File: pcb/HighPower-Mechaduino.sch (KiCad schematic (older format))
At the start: 31 parts, among them J1 SUPPLY, J2 STEPPER, P1 SWD, Q1 SSM3J328R, Q2 BSS138, SW1 SW_PUSH, U1 AS5047D, U2 AP2112K-3.3TRG1, U3 AT24CS64-SSHM

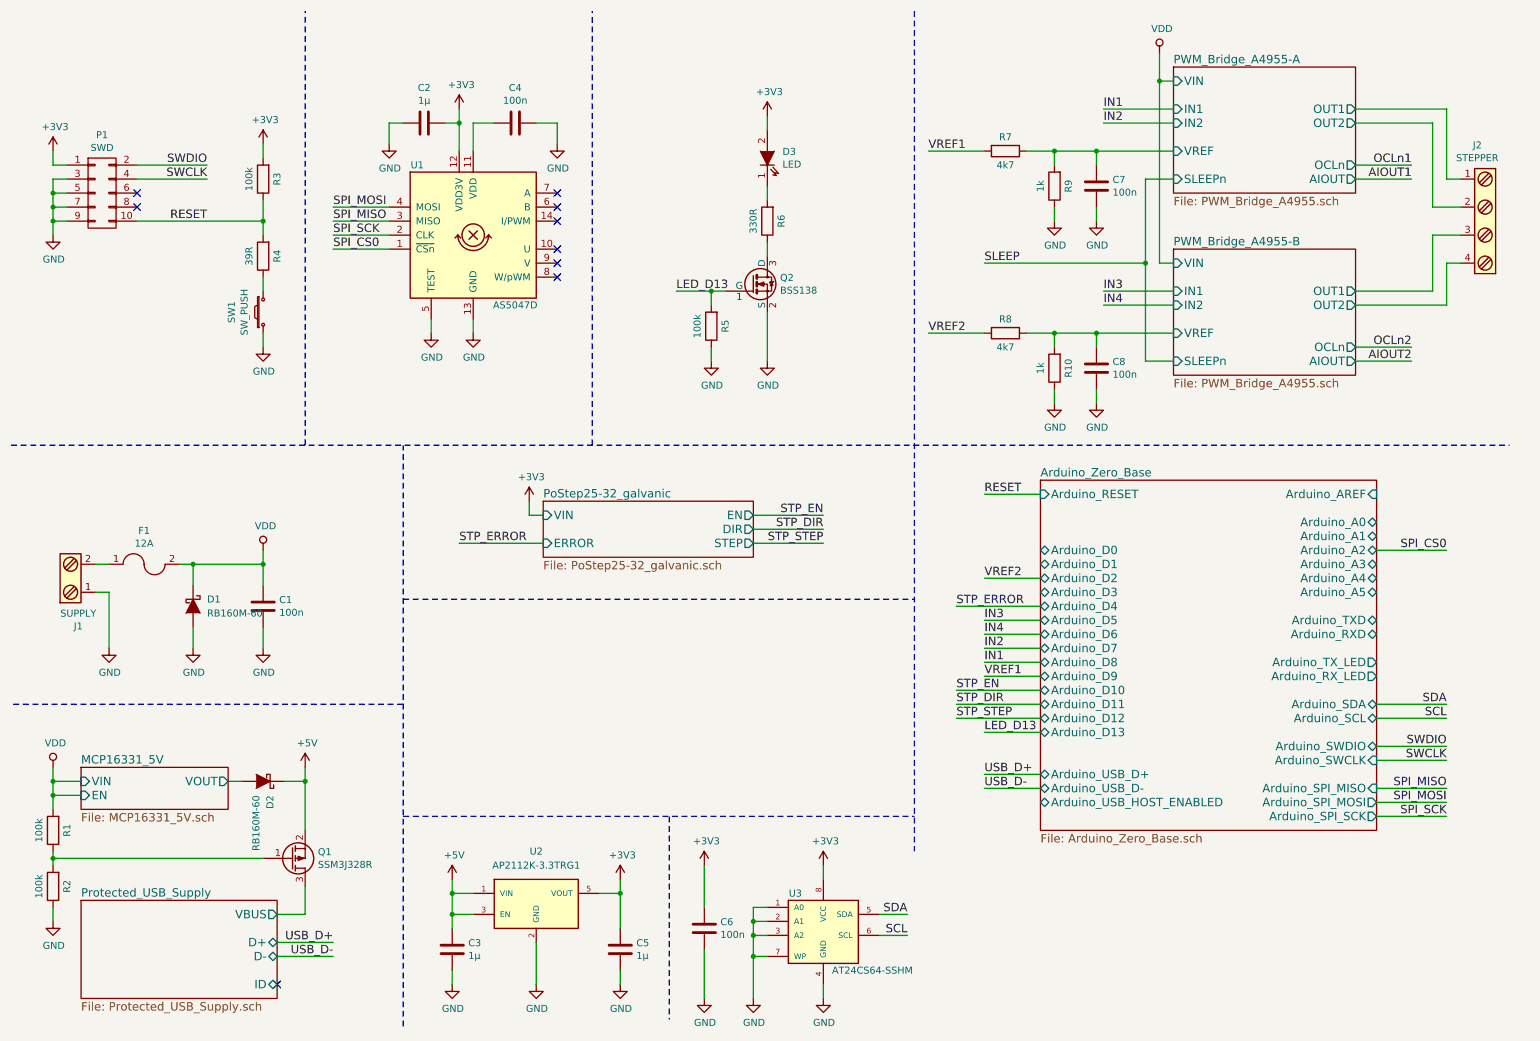
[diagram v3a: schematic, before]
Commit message: Improve pcb routing, add testpoints and etc. The design improves a lot. Still lots to do, but most important design parts should now be drafted almost complete.
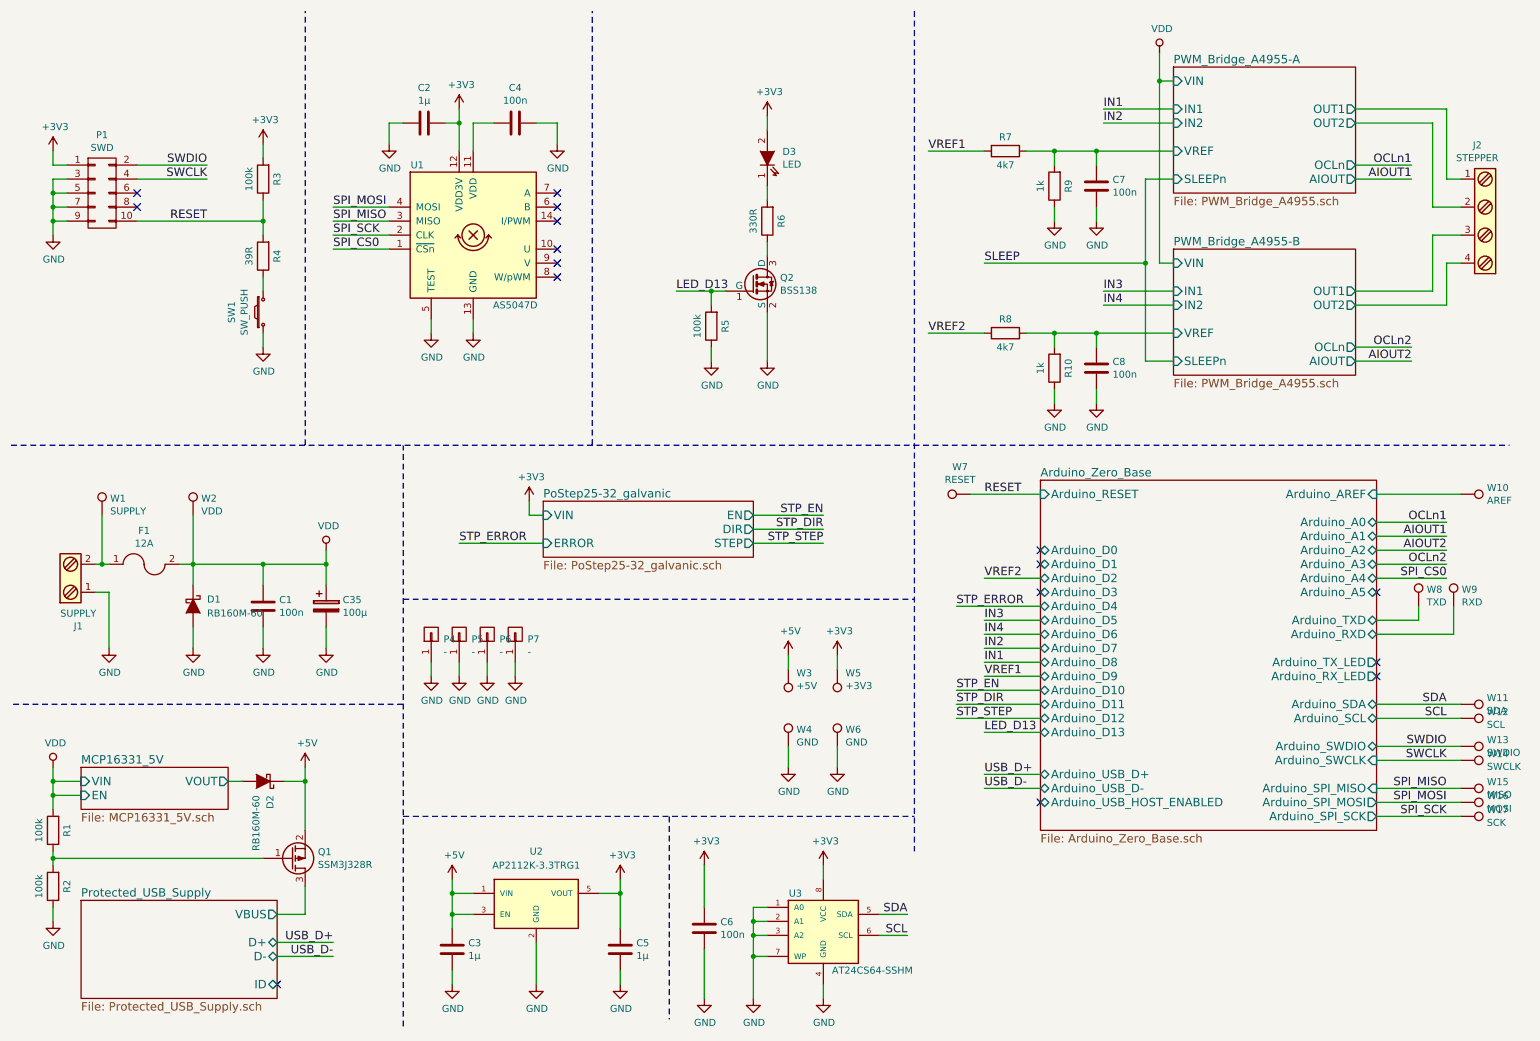
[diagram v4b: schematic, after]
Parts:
- added C35: 100µ, Capacitors_SMD:c_elec_10x10, symbol CP
- added P4, P5, P6, P7: -, Mounting_Holes:MountingHole_4.3mm_M4_Pad_Via, symbol CONN_01X01
- added W1: SUPPLY, Measurement_Points:Measurement_Point_Round-SMD-Pad_Small, symbol TEST_1P
- added W10: AREF, Measurement_Points:Measurement_Point_Round-SMD-Pad_Small, symbol TEST_1P
- added W11: SDA, Measurement_Points:Measurement_Point_Round-SMD-Pad_Small, symbol TEST_1P
- added W12: SCL, Measurement_Points:Measurement_Point_Round-SMD-Pad_Small, symbol TEST_1P
- added W13: SWDIO, Measurement_Points:Measurement_Point_Round-SMD-Pad_Small, symbol TEST_1P
- added W14: SWCLK, Measurement_Points:Measurement_Point_Round-SMD-Pad_Small, symbol TEST_1P
- added W15: MISO, Measurement_Points:Measurement_Point_Round-SMD-Pad_Small, symbol TEST_1P
- added W16: MOSI, Measurement_Points:Measurement_Point_Round-SMD-Pad_Small, symbol TEST_1P
- added W17: SCK, Measurement_Points:Measurement_Point_Round-SMD-Pad_Small, symbol TEST_1P
- added W2: VDD, Measurement_Points:Measurement_Point_Round-SMD-Pad_Small, symbol TEST_1P
- added W3: +5V, Measurement_Points:Measurement_Point_Round-SMD-Pad_Small, symbol TEST_1P
- added W4, W6: GND, Measurement_Points:Measurement_Point_Round-SMD-Pad_Small, symbol TEST_1P
- added W5: +3V3, Measurement_Points:Measurement_Point_Round-SMD-Pad_Small, symbol TEST_1P
- added W7: RESET, Measurement_Points:Measurement_Point_Round-SMD-Pad_Small, symbol TEST_1P
- added W8: TXD, Measurement_Points:Measurement_Point_Round-SMD-Pad_Small, symbol TEST_1P
- added W9: RXD, Measurement_Points:Measurement_Point_Round-SMD-Pad_Small, symbol TEST_1P
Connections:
- net +3V3: now also W5.1
- net +5V: now also W3.1
- net Arduino_Zero_Base/Arduino_AREF: now also W10.1
- net Arduino_Zero_Base/Arduino_RXD: now also W9.1
- net Arduino_Zero_Base/Arduino_TXD: now also W8.1
- net GND: now also C35.2, P4.1 (P1), P5.1 (P1), P6.1 (P1), P7.1 (P1), W4.1, W6.1
- net RESET: now also W7.1
- net SCL: now also W12.1
- net SDA: now also W11.1
- net SPI_MISO: now also W15.1
- net SPI_MOSI: now also W16.1
- net SPI_SCK: now also W17.1
- net SWCLK: now also W14.1
- net SWDIO: now also W13.1
- net VDD: now also C35.1, W2.1
- net at F1.1, J1.2: now also W1.1
- no-connect marks 9 -> 16

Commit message: Improve pcb
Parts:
- F1: footprint Fuse_Holders_and_Fuses:Fuseholder5x20_horiz_open_inline_Type-I -> Fuse_Holders_and_Fuses_local:Fuse_0679H
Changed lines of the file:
@@
 F 0 "F1" H 1450 4690 50  0000 C CNN
 F 1 "12A" H 1450 4599 50  0000 C CNN
-F 2 "Fuse_Holders_and_Fuses:Fuseholder5x20_horiz_open_inline_Type-I" H 1450 4450 50  0001 C CNN
+F 2 "Fuse_Holders_and_Fuses_local:Fuse_0679H" H 1450 4450 50  0001 C CNN
 F 3 "" H 1450 4450 50  0000 C CNN
 	1    1450 4450

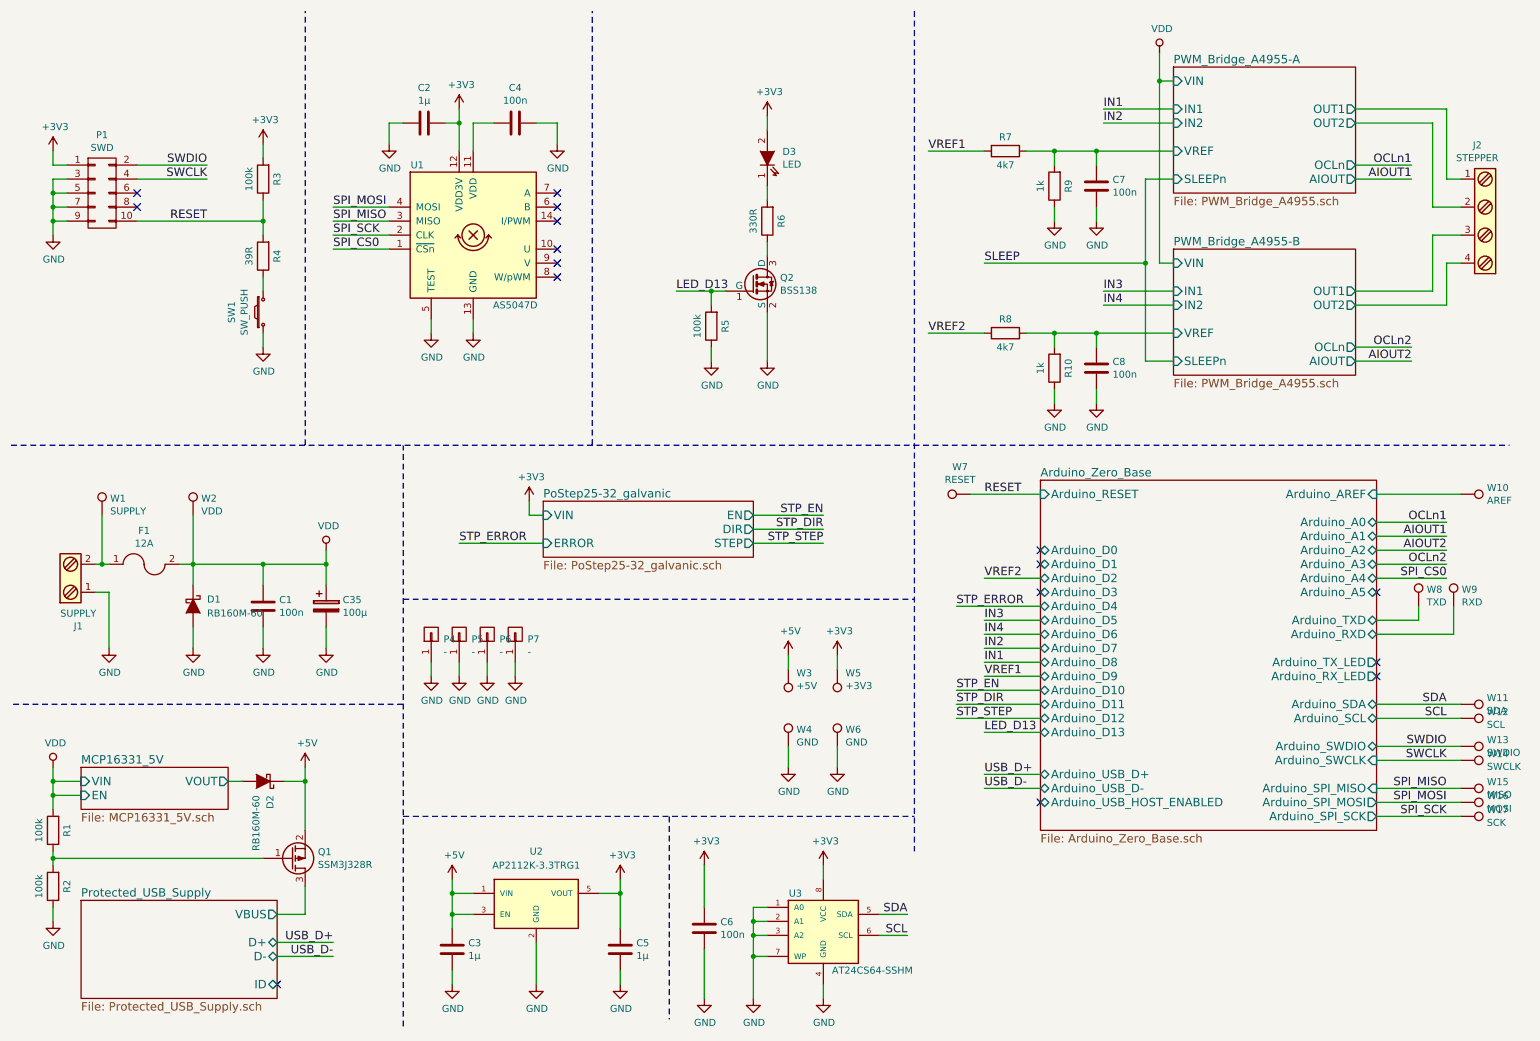
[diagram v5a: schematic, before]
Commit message: Improve board routing, add some dukos
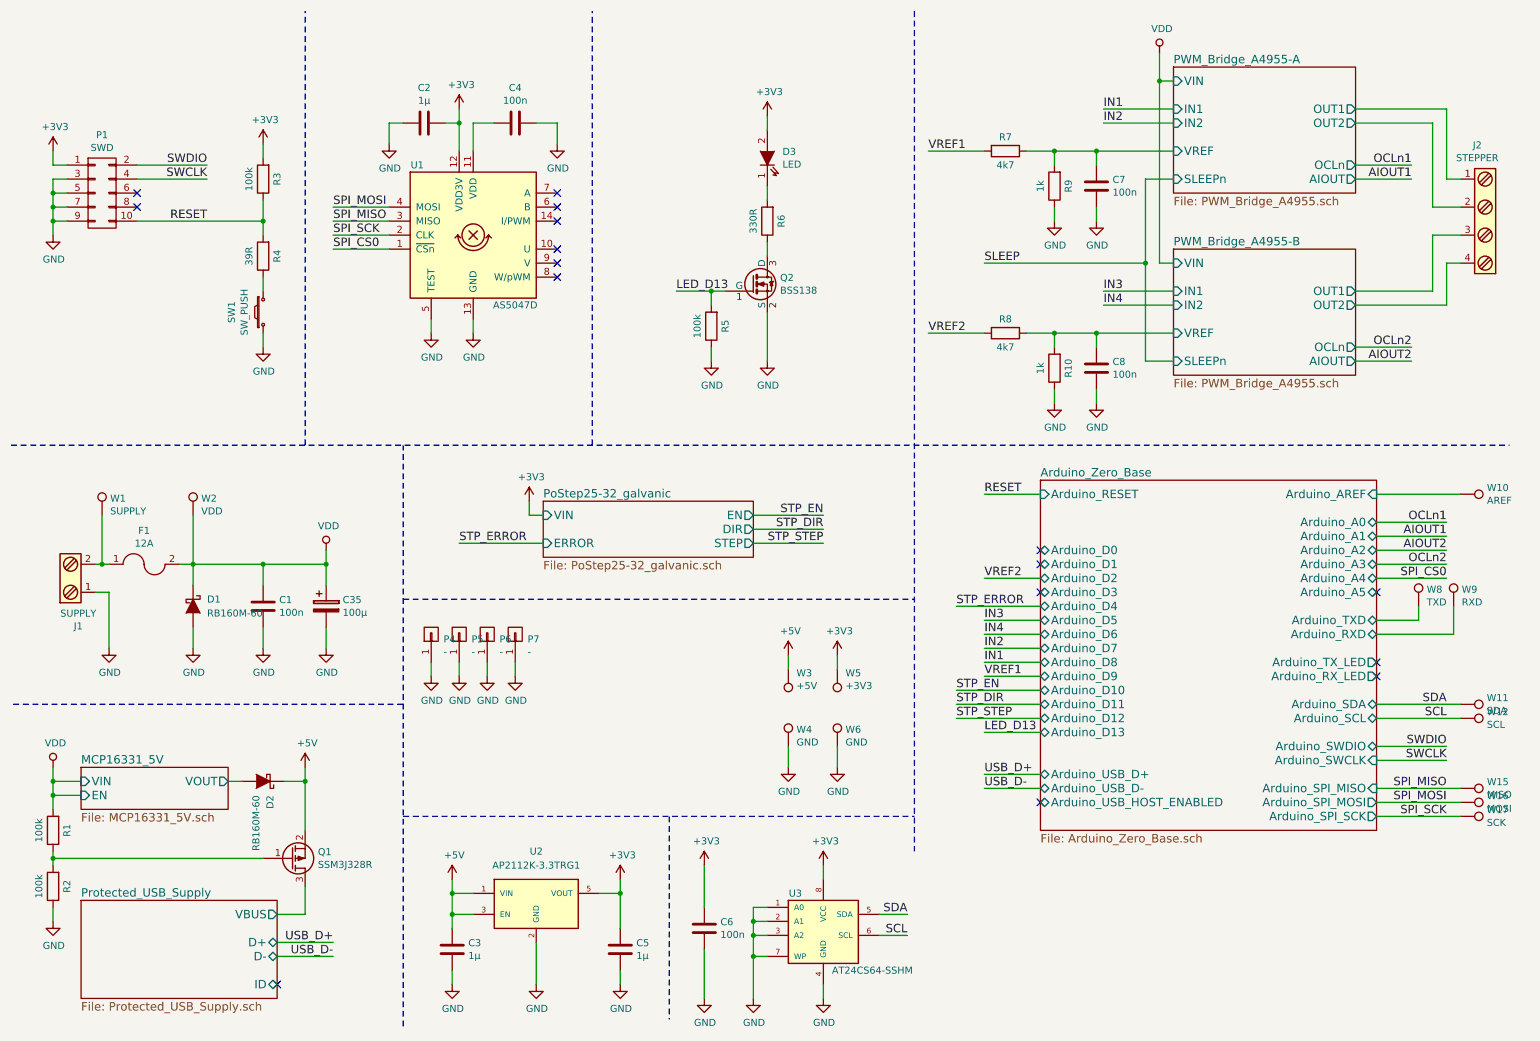
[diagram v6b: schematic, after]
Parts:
- removed W13: SWDIO, Measurement_Points:Measurement_Point_Round-SMD-Pad_Small, symbol TEST_1P
- removed W14: SWCLK, Measurement_Points:Measurement_Point_Round-SMD-Pad_Small, symbol TEST_1P
- removed W7: RESET, Measurement_Points:Measurement_Point_Round-SMD-Pad_Small, symbol TEST_1P
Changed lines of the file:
@@
 	3800 1300 3800 1500
 Wire Wire Line
-	3700 1200 3700 1500
+	3700 1200 3700 1300
+Wire Wire Line
+	3700 1300 3700 1500
 Wire Wire Line
 	3700 1300 3600 1300
@@
 	8700 2300 8800 2300
 Wire Wire Line
-	8700 800  8700 2300
+	8700 800  8700 1000
+Wire Wire Line
+	8700 1000 8700 2300
 Wire Wire Line
 	8700 1000 8800 1000
@@
 	8600 3000 8800 3000
 Wire Wire Line
-	8600 1700 8600 3000
+	8600 1700 8600 2300
+Wire Wire Line
+	8600 2300 8600 3000
 Wire Wire Line
 	8600 1700 8800 1700
@@
 $EndComp
 Wire Wire Line
-	7750 2800 8800 2800
+	7750 2800 7950 2800
+Wire Wire Line
+	7950 2800 8250 2800
+Wire Wire Line
+	8250 2800 8800 2800
 Wire Wire Line
 	7450 1500 7050 1500
@@
 	1200 4650 1200 5050
 Wire Wire Line
-	1200 4450 1100 4450
-Wire Wire Line
-	1700 4450 2750 4450
-Wire Wire Line
-	1800 4100 1800 4600
+	1200 4450 1150 4450
+Wire Wire Line
+	1150 4450 1100 4450
+Wire Wire Line
+	1700 4450 1800 4450
+Wire Wire Line
+	1800 4450 2300 4450
+Wire Wire Line
+	2300 4450 2750 4450
+Wire Wire Line
+	1800 4100 1800 4450
+Wire Wire Line
+	1800 4450 1800 4600
 Wire Wire Line
 	1800 4900 1800 5050
@@
 $EndComp
 Wire Wire Line
-	2750 4350 2750 4600
+	2750 4350 2750 4450
+Wire Wire Line
+	2750 4450 2750 4600
 Connection ~ 1800 4450
 Wire Wire Line
@@
 $EndComp
 Wire Wire Line
-	3650 6700 3650 7050
+	3650 6700 3650 6800
+Wire Wire Line
+	3650 6800 3650 6950
+Wire Wire Line
+	3650 6950 3650 7050
 $Comp
 L GND #PWR017
@@
 	4700 6800 4850 6800
 Wire Wire Line
-	4850 6700 4850 7050
+	4850 6700 4850 6800
+Wire Wire Line
+	4850 6800 4850 7050
 Wire Wire Line
 	4850 7350 4850 7450
@@
 	900  1700 800  1700
 Wire Wire Line
-	800  1700 800  2100
+	800  1700 800  1800
+Wire Wire Line
+	800  1800 800  1900
+Wire Wire Line
+	800  1900 800  2000
+Wire Wire Line
+	800  2000 800  2100
 Wire Wire Line
 	800  2000 900  2000
@@
 SWCLK
 Wire Wire Line
-	10250 5750 10850 5750
-Wire Wire Line
-	10250 5850 10850 5850
+	10250 5750 10750 5750
+Wire Wire Line
+	10250 5850 10750 5850
 Text Label 10750 5750 2    60   ~ 0
 SWDIO
@@
 	2300 1550 2300 1450
 Wire Wire Line
-	2300 1850 2300 2100
+	2300 1850 2300 2000
+Wire Wire Line
+	2300 2000 2300 2100
 $Comp
 L GND #PWR024
@@
 RESET
 Wire Wire Line
-	7350 3950 7850 3950
+	7450 3950 7850 3950
 Text Label 7450 3950 0    60   ~ 0
 RESET
@@
 $EndComp
 Wire Wire Line
-	5250 2500 5600 2500
+	5250 2500 5500 2500
+Wire Wire Line
+	5500 2500 5600 2500
 Wire Wire Line
 	5500 2500 5500 2600
@@
 	1000 6000 800  6000
 Wire Wire Line
-	800  5900 800  6200
+	800  5900 800  6000
+Wire Wire Line
+	800  6000 800  6100
+Wire Wire Line
+	800  6100 800  6200
 Wire Wire Line
 	800  6100 1000 6100
@@
 	2450 6000 2600 6000
 Wire Wire Line
-	2600 5900 2600 6350
+	2600 5900 2600 6000
+Wire Wire Line
+	2600 6000 2600 6350
 Connection ~ 2600 6000
 $Comp
@@
 	800  7000 800  6900
 Wire Wire Line
-	800  6500 800  6600
+	800  6500 800  6550
+Wire Wire Line
+	800  6550 800  6600
 Connection ~ 800  6100
 Wire Wire Line
@@
 	5900 6900 5800 6900
 Wire Wire Line
-	5800 6900 5800 7550
+	5800 6900 5800 7000
+Wire Wire Line
+	5800 7000 5800 7100
+Wire Wire Line
+	5800 7100 5800 7250
+Wire Wire Line
+	5800 7250 5800 7550
 Wire Wire Line
 	5900 7000 5800 7000
@@
 $EndComp
 Wire Wire Line
-	7750 1500 8800 1500
+	7750 1500 7950 1500
+Wire Wire Line
+	7950 1500 8250 1500
+Wire Wire Line
+	8250 1500 8800 1500
 Wire Wire Line
 	8250 1600 8250 1500
@@
 	6050 5100 6050 5200
 $Comp
-L TEST_1P W7
-U 1 1 5817C652
-P 7350 3950
-F 0 "W7" V 7545 4024 50  0000 C CNN
-F 1 "RESET" V 7454 4024 50  0000 C CNN
-F 2 "Measurement_Points:Measurement_Point_Round-SMD-Pad_Small" H 7550 3950 50  0001 C CNN
-F 3 "" H 7550 3950 50  0000 C CNN
-	1    7350 3950
-	0    -1   -1   0
-$EndComp
-$Comp
-L TEST_1P W13
-U 1 1 5817E778
-P 10850 5750
-F 0 "W13" V 10804 5938 50  0000 L CNN
-F 1 "SWDIO" V 10895 5938 50  0000 L CNN
-F 2 "Measurement_Points:Measurement_Point_Round-SMD-Pad_Small" H 11050 5750 50  0001 C CNN
-F 3 "" H 11050 5750 50  0000 C CNN
-	1    10850 5750
-	0    1    1    0
-$EndComp
-$Comp
-L TEST_1P W14
-U 1 1 5817F7BB
-P 10850 5850
-F 0 "W14" V 10804 6038 50  0000 L CNN
-F 1 "SWCLK" V 10895 6038 50  0000 L CNN
-F 2 "Measurement_Points:Measurement_Point_Round-SMD-Pad_Small" H 11050 5850 50  0001 C CNN
-F 3 "" H 11050 5850 50  0000 C CNN
-	1    10850 5850
-	0    1    1    0
-$EndComp
-$Comp
 L TEST_1P W11
